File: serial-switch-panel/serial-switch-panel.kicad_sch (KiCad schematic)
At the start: 59 parts, among them J10 Conn_01x01, J11 Conn_01x01, J12 Conn_01x01, J13 Conn_01x01, J14 Conn_01x01, J15 Conn_01x01, J16 Conn_01x01, J17 Conn_01x01, J18 Conn_01x01, J2 2501551-4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

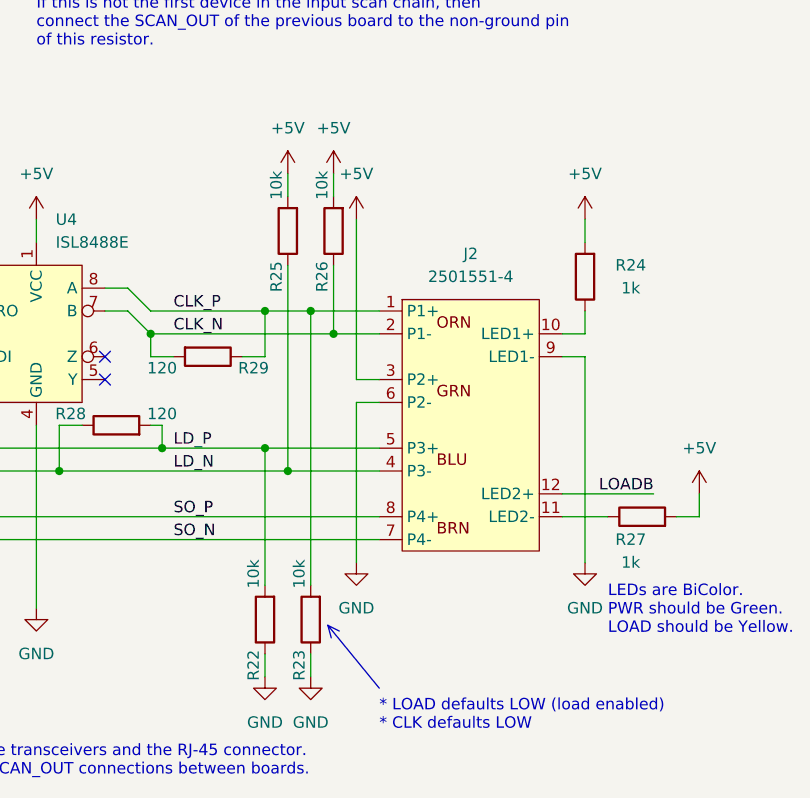
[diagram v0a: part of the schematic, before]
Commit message: Fix front-panel sch ERC
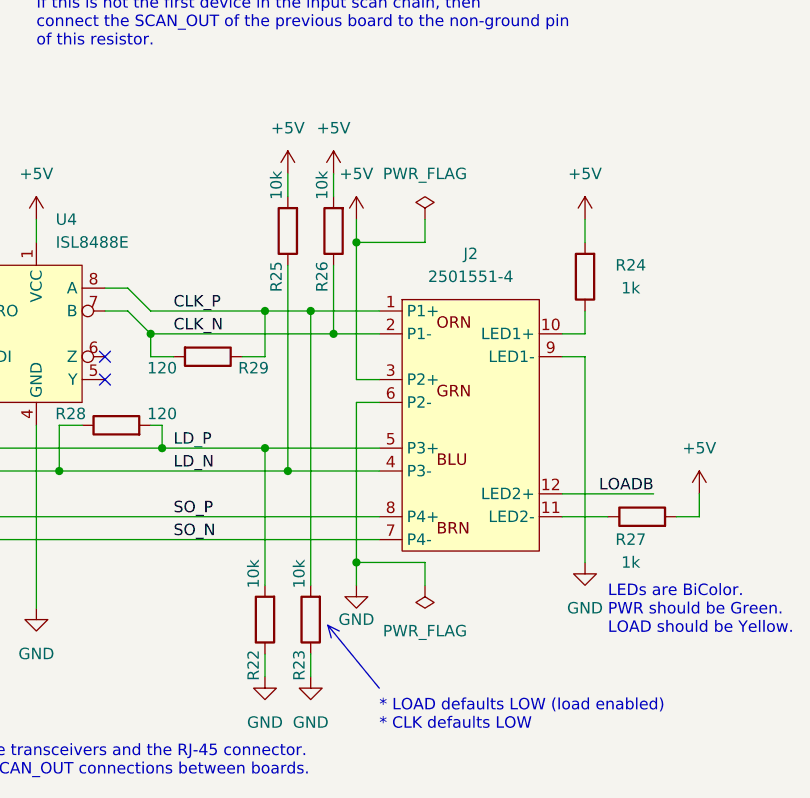
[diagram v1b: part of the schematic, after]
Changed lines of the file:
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@@
 	)
 	(junction
+		(at 119.38 167.64)
+		(diameter 0)
+		(color 0 0 0 0)
+	)
+	(junction
 		(at 116.84 142.24)
 		(diameter 0)
@@
 	)
 	(junction
+		(at 119.38 132.08)
+		(diameter 0)
+		(color 0 0 0 0)
+	)
+	(junction
 		(at 60.96 86.36)
 		(diameter 0)
@@
 	(wire
 		(pts
+			(xy 127 129.54) (xy 127 132.08)
+		)
+		(stroke
+			(width 0)
+			(type default)
+		)
+	)
+	(wire
+		(pts
 			(xy 30.48 58.42) (xy 33.02 58.42)
 		)
@@
 	(wire
 		(pts
+			(xy 119.38 132.08) (xy 119.38 147.32)
+		)
+		(stroke
+			(width 0)
+			(type default)
+		)
+	)
+	(wire
+		(pts
 			(xy 30.48 66.04) (xy 33.02 66.04)
 		)
@@
 		)
 	)
+	(wire
+		(pts
+			(xy 119.38 170.18) (xy 119.38 167.64)
+		)
+		(stroke
+			(width 0)
+			(type default)
+		)
+	)
 	(polyline
 		(pts
@@
 	(wire
 		(pts
+			(xy 127 170.18) (xy 127 167.64)
+		)
+		(stroke
+			(width 0)
+			(type default)
+		)
+	)
+	(wire
+		(pts
 			(xy 116.84 142.24) (xy 121.92 142.24)
 		)
@@
 	(wire
 		(pts
+			(xy 127 167.64) (xy 119.38 167.64)
+		)
+		(stroke
+			(width 0)
+			(type default)
+		)
+	)
+	(wire
+		(pts
 			(xy 40.64 55.88) (xy 66.04 55.88)
 		)
@@
 	(wire
 		(pts
-			(xy 119.38 129.54) (xy 119.38 147.32)
+			(xy 119.38 129.54) (xy 119.38 132.08)
 		)
 		(stroke
@@
 	(wire
 		(pts
+			(xy 127 132.08) (xy 119.38 132.08)
+		)
+		(stroke
+			(width 0)
+			(type default)
+		)
+	)
+	(wire
+		(pts
 			(xy 96.52 142.24) (xy 116.84 142.24)
 		)
@@
 	(symbol
 		(lib_id "power:GND")
-		(at 119.38 167.64 0)
+		(at 119.38 170.18 0)
 		(unit 1)
 		(body_style 1)
@@
 		(in_pos_files yes)
 		(dnp no)
-		(fields_autoplaced yes)
 		(property "Reference" "#PWR022"
-			(at 119.38 173.99 0)
+			(at 119.38 176.53 0)
 			(hide yes)
 			(show_name no)
@@
 		)
 		(property "Value" "GND"
-			(at 119.38 172.72 0)
+			(at 119.38 173.99 0)
 			(show_name no)
 			(do_not_autoplace no)
@@
 		)
 		(property "Footprint" ""
-			(at 119.38 167.64 0)
+			(at 119.38 170.18 0)
 			(hide yes)
 			(show_name no)
@@
 		)
 		(property "Datasheet" ""
-			(at 119.38 167.64 0)
+			(at 119.38 170.18 0)
 			(hide yes)
 			(show_name no)
@@
 		)
 		(property "Description" "Power symbol creates a global label with name \"GND\" , ground"
-			(at 119.38 167.64 0)
+			(at 119.38 170.18 0)
 			(hide yes)
 			(show_name no)
@@
 	)
 	(symbol
+		(lib_id "power:PWR_FLAG")
+		(at 127 170.18 0)
+		(mirror x)
+		(unit 1)
+		(body_style 1)
+		(exclude_from_sim no)
+		(in_bom yes)
+		(on_board yes)
+		(in_pos_files yes)
+		(dnp no)
+		(fields_autoplaced yes)
+		(property "Reference" "#FLG02"
+			(at 127 172.085 0)
+			(hide yes)
+			(show_name no)
+			(do_not_autoplace no)
+			(effects
+				(font
+					(size 1.27 1.27)
+				)
+			)
+		)
+		(property "Value" "PWR_FLAG"
+			(at 127 175.26 0)
+			(show_name no)
+			(do_not_autoplace no)
+			(effects
+				(font
+					(size 1.27 1.27)
+				)
+			)
+		)
+		(property "Footprint" ""
+			(at 127 170.18 0)
+			(hide yes)
+			(show_name no)
+			(do_not_autoplace no)
+			(effects
+				(font
+					(size 1.27 1.27)
+				)
+			)
+		)
+		(property "Datasheet" ""
+			(at 127 170.18 0)
+			(hide yes)
+			(show_name no)
+			(do_not_autoplace no)
+			(effects
+				(font
+					(size 1.27 1.27)
+				)
+			)
+		)
+		(property "Description" "Special symbol for telling ERC where power comes from"
+			(at 127 170.18 0)
+			(hide yes)
+			(show_name no)
+			(do_not_autoplace no)
+			(effects
+				(font
+					(size 1.27 1.27)
+				)
+			)
+		)
+		(pin "1"
+		)
+		(instances
+			(project "serial-switch-panel"
+				(path "/6e8e0d39-e51b-4511-a712-1d92a774977f"
+					(reference "#FLG02")
+					(unit 1)
+				)
+			)
+		)
+	)
+	(symbol
 		(lib_id "CUSTOM:C_Polarized")
 		(at 243.84 144.78 0)
@@
 					(unit 1)
 				)
+			)
+		)
+	)
+	(symbol
+		(lib_id "power:PWR_FLAG")
+		(at 127 129.54 0)
+		(unit 1)
+		(body_style 1)
+		(exclude_from_sim no)
+		(in_bom yes)
+		(on_board yes)
+		(in_pos_files yes)
+		(dnp no)
+		(fields_autoplaced yes)
+		(property "Reference" "#FLG01"
+			(at 127 127.635 0)
+			(hide yes)
+			(show_name no)
+			(do_not_autoplace no)
+			(effects
+				(font
+					(size 1.27 1.27)
+				)
+			)
+		)
+		(property "Value" "PWR_FLAG"
+			(at 127 124.46 0)
+			(show_name no)
+			(do_not_autoplace no)
+			(effects
+				(font
+					(size 1.27 1.27)
+				)
+			)
+		)
+		(property "Footprint" ""
+			(at 127 129.54 0)
+			(hide yes)
+			(show_name no)
+			(do_not_autoplace no)
+			(effects
+				(font
+					(size 1.27 1.27)
+				)
+			)
+		)
+		(property "Datasheet" ""
+			(at 127 129.54 0)
+			(hide yes)
+			(show_name no)
+			(do_not_autoplace no)
+			(effects
+				(font
+					(size 1.27 1.27)
+				)
+			)
+		)
+		(property "Description" "Special symbol for telling ERC where power comes from"
+			(at 127 129.54 0)
+			(hide yes)
+			(show_name no)
+			(do_not_autoplace no)
+			(effects
+				(font
+					(size 1.27 1.27)
+				)
+			)
+		)
+		(pin "1"
+		)
+		(instances
+			(project ""
+				(path "/6e8e0d39-e51b-4511-a712-1d92a774977f"
+					(reference "#FLG01")
+					(unit 1)
+				)

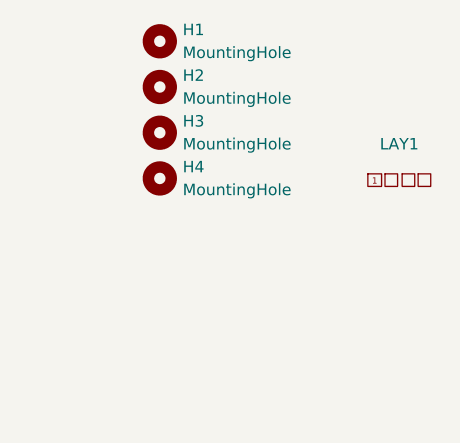
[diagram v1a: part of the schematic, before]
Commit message: Rough front-panel placement
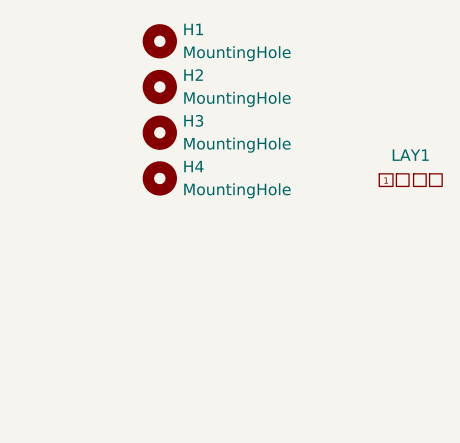
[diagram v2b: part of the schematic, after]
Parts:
- removed LAY1: (no value), custom_footprints:Layer_Indicator_4, symbol Custom:Layer_Indicator
- added LAY1: (no value), Symbol:LayerMarker_2_3.81x2.54mm_TextH1mm_P1.27mm_BottomMirrored, symbol CUSTOM:Layer_Indicator
- J10, J11, J12, J13, J14, J15, J16, J17, J18, J3, J4, J5, J6, J7, J8, J9: footprint (none) -> CUSTOM:Pin_D1.0mm
- J2: footprint (none) -> CUSTOM:2501551-4
- U1: footprint (none) -> Package_SO:Texas_DYY0016A_TSOT-23-16_2x4.2mm_P0.5mm
- U3: footprint (none) -> Package_SO:TSOP-5_1.65x3.05mm_P0.95mm
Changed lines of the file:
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@@
 			)
 		)
-		(property "Footprint" ""
+		(property "Footprint" "CUSTOM:Pin_D1.0mm"
 			(at 241.3 106.68 0)
 			(hide yes)
@@
 			)
 		)
-		(property "Footprint" ""
+		(property "Footprint" "CUSTOM:Pin_D1.0mm"
 			(at 48.26 170.18 0)
 			(hide yes)
@@
 			)
 		)
-		(property "Footprint" ""
+		(property "Footprint" "CUSTOM:Pin_D1.0mm"
 			(at 25.4 58.42 0)
 			(hide yes)
@@
 	)
 	(symbol
+		(lib_id "CUSTOM:Layer_Indicator")
+		(at 271.78 38.1 0)
+		(unit 1)
+		(body_style 1)
+		(exclude_from_sim no)
+		(in_bom no)
+		(on_board yes)
+		(in_pos_files yes)
+		(dnp no)
+		(fields_autoplaced yes)
+		(property "Reference" "LAY1"
+			(at 271.7165 35.56 0)
+			(show_name no)
+			(do_not_autoplace no)
+			(effects
+				(font
+					(size 1.27 1.27)
+				)
+			)
+		)
+		(property "Value" ""
+			(at 271.7165 35.56 0)
+			(show_name no)
+			(do_not_autoplace no)
+			(effects
+				(font
+					(size 1.27 1.27)
+				)
+			)
+		)
+		(property "Footprint" "Symbol:LayerMarker_2_3.81x2.54mm_TextH1mm_P1.27mm_BottomMirrored"
+			(at 270.764 36.322 0)
+			(hide yes)
+			(show_name no)
+			(do_not_autoplace no)
+			(effects
+				(font
+					(size 1.27 1.27)
+				)
+			)
+		)
+		(property "Datasheet" ""
+			(at 270.764 36.322 0)
+			(hide yes)
+			(show_name no)
+			(do_not_autoplace no)
+			(effects
+				(font
+					(size 1.27 1.27)
+				)
+			)
+		)
+		(property "Description" ""
+			(at 270.764 36.322 0)
+			(hide yes)
+			(show_name no)
+			(do_not_autoplace no)
+			(effects
+				(font
+					(size 1.27 1.27)
+				)
+			)
+		)
+		(instances
+			(project ""
+				(path "/6e8e0d39-e51b-4511-a712-1d92a774977f"
+					(reference "LAY1")
+					(unit 1)
+				)
+			)
+		)
+	)
+	(symbol
 		(lib_id "CUSTOM:R")
 		(at 71.12 78.74 180)
@@
 			)
 		)
-		(property "Footprint" ""
+		(property "Footprint" "CUSTOM:Pin_D1.0mm"
 			(at 129.54 50.8 0)
 			(hide yes)
@@
 			)
 		)
-		(property "Footprint" ""
+		(property "Footprint" "CUSTOM:Pin_D1.0mm"
 			(at 25.4 63.5 0)
 			(hide yes)
@@
 			)
 		)
-		(property "Footprint" ""
+		(property "Footprint" "CUSTOM:Pin_D1.0mm"
 			(at 25.4 48.26 0)
 			(hide yes)
@@
 			)
 		)
-		(property "Footprint" ""
+		(property "Footprint" "CUSTOM:Pin_D1.0mm"
 			(at 25.4 55.88 0)
 			(hide yes)
@@
 			)
 		)
-		(property "Footprint" ""
+		(property "Footprint" "CUSTOM:2501551-4"
 			(at 132.08 152.4 0)
 			(hide yes)
@@
 			)
 		)
-		(property "Footprint" ""
+		(property "Footprint" "Package_SO:Texas_DYY0016A_TSOT-23-16_2x4.2mm_P0.5mm"
 			(at 109.22 63.5 0)
 			(hide yes)
@@
 			)
 		)
-		(property "Footprint" ""
+		(property "Footprint" "CUSTOM:Pin_D1.0mm"
 			(at 25.4 50.8 0)
 			(hide yes)
@@
 			)
 		)
-		(property "Footprint" ""
+		(property "Footprint" "CUSTOM:Pin_D1.0mm"
 			(at 25.4 101.6 0)
 			(hide yes)
@@
 			)
 		)
-		(property "Footprint" ""
+		(property "Footprint" "CUSTOM:Pin_D1.0mm"
 			(at 25.4 106.68 0)
 			(hide yes)
@@
 			)
 		)
-		(property "Footprint" ""
+		(property "Footprint" "CUSTOM:Pin_D1.0mm"
 			(at 73.66 132.08 0)
 			(hide yes)
@@
 			)
 		)
-		(property "Footprint" ""
+		(property "Footprint" "CUSTOM:Pin_D1.0mm"
 			(at 25.4 60.96 0)
 			(hide yes)
@@
 	)
 	(symbol
-		(lib_id "Custom:Layer_Indicator")
-		(at 270.51 38.1 0)
-		(unit 1)
-		(body_style 1)
-		(exclude_from_sim no)
-		(in_bom no)
-		(on_board yes)
-		(in_pos_files yes)
-		(dnp no)
-		(fields_autoplaced yes)
-		(property "Reference" "LAY1"
-			(at 270.4465 34.29 0)
-			(show_name no)
-			(do_not_autoplace no)
-			(effects
-				(font
-					(size 1.27 1.27)
-				)
-			)
-		)
-		(property "Value" ""
-			(at 270.4465 35.56 0)
-			(show_name no)
-			(do_not_autoplace no)
-			(effects
-				(font
-					(size 1.27 1.27)
-				)
-			)
-		)
-		(property "Footprint" "custom_footprints:Layer_Indicator_4"
-			(at 269.494 36.322 0)
-			(hide yes)
-			(show_name no)
-			(do_not_autoplace no)
-			(effects
-				(font
-					(size 1.27 1.27)
-				)
-			)
-		)
-		(property "Datasheet" ""
-			(at 269.494 36.322 0)
-			(hide yes)
-			(show_name no)
-			(do_not_autoplace no)
-			(effects
-				(font
-					(size 1.27 1.27)
-				)
-			)
-		)
-		(property "Description" ""
-			(at 269.494 36.322 0)
-			(hide yes)
-			(show_name no)
-			(do_not_autoplace no)
-			(effects
-				(font
-					(size 1.27 1.27)
-				)
-			)
-		)
-		(instances
-			(project "serial-switch-panel"
-				(path "/6e8e0d39-e51b-4511-a712-1d92a774977f"
-					(reference "LAY1")
-					(unit 1)
-				)
-			)
-		)
-	)
-	(symbol
 		(lib_id "CUSTOM:C")
 		(at 182.88 144.78 0)
@@
 			)
 		)
-		(property "Footprint" ""
+		(property "Footprint" "Package_SO:TSOP-5_1.65x3.05mm_P0.95mm"
 			(at 167.64 48.26 0)
 			(hide yes)
@@
 			)
 		)
-		(property "Footprint" ""
+		(property "Footprint" "CUSTOM:Pin_D1.0mm"
 			(at 48.26 149.86 0)
 			(hide yes)
@@
 			)
 		)
-		(property "Footprint" ""
+		(property "Footprint" "CUSTOM:Pin_D1.0mm"
 			(at 241.3 101.6 0)
 			(hide yes)
@@
 			)
 		)
-		(property "Footprint" ""
+		(property "Footprint" "CUSTOM:Pin_D1.0mm"
 			(at 25.4 53.34 0)
 			(hide yes)
@@
 			)
 		)
-		(property "Footprint" ""
+		(property "Footprint" "CUSTOM:Pin_D1.0mm"
 			(at 25.4 66.04 0)
 			(hide yes)

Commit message: [fp] Correct P4+/- swap in ethernet connector
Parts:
- C2: footprint Capacitor_SMD:C_1206_3216Metric -> Capacitor_THT:C_Radial_D8.0mm_H7.0mm_P3.50mm
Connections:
- net SO_N: now also J2.8 (P4-), U2.5 (Y); no longer J2.7 (P4-), U2.6 (Z)
- net SO_P: now also J2.7 (P4+), U2.6 (Z); no longer J2.8 (P4+), U2.5 (Y)
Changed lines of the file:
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@@
 	(wire
 		(pts
-			(xy 66.04 162.56) (xy 71.12 162.56)
-		)
-		(stroke
-			(width 0)
-			(type default)
-		)
-	)
-	(wire
-		(pts
 			(xy 66.04 157.48) (xy 86.36 157.48)
 		)
@@
 	(wire
 		(pts
-			(xy 73.66 165.1) (xy 121.92 165.1)
-		)
-		(stroke
-			(width 0)
-			(type default)
-		)
-	)
-	(wire
-		(pts
 			(xy 58.42 63.5) (xy 58.42 73.66)
 		)
@@
 	(wire
 		(pts
-			(xy 71.12 162.56) (xy 73.66 165.1)
-		)
-		(stroke
-			(width 0)
-			(type default)
-		)
-	)
-	(wire
-		(pts
 			(xy 58.42 86.36) (xy 60.96 86.36)
 		)
@@
 	(wire
 		(pts
+			(xy 66.04 162.56) (xy 121.92 162.56)
+		)
+		(stroke
+			(width 0)
+			(type default)
+		)
+	)
+	(wire
+		(pts
 			(xy 30.48 63.5) (xy 33.02 63.5)
 		)
@@
 	(wire
 		(pts
-			(xy 66.04 165.1) (xy 71.12 165.1)
-		)
-		(stroke
-			(width 0)
-			(type default)
-		)
-	)
-	(wire
-		(pts
 			(xy 121.92 45.72) (xy 152.4 45.72)
 		)
@@
 	(wire
 		(pts
+			(xy 66.04 165.1) (xy 121.92 165.1)
+		)
+		(stroke
+			(width 0)
+			(type default)
+		)
+	)
+	(wire
+		(pts
 			(xy 228.6 139.7) (xy 228.6 142.24)
 		)
@@
 	(wire
 		(pts
-			(xy 73.66 162.56) (xy 121.92 162.56)
-		)
-		(stroke
-			(width 0)
-			(type default)
-		)
-	)
-	(wire
-		(pts
 			(xy 40.64 66.04) (xy 55.88 66.04)
 		)
@@
 		)
 	)
-	(wire
-		(pts
-			(xy 71.12 165.1) (xy 73.66 162.56)
-		)
-		(stroke
-			(width 0)
-			(type default)
-		)
-	)
 	(label "IN_A"
 		(at 45.72 48.26 0)
@@
 			)
 		)
-		(property "Footprint" "Capacitor_SMD:C_1206_3216Metric"
+		(property "Footprint" "Capacitor_THT:C_Radial_D8.0mm_H7.0mm_P3.50mm"
 			(at 244.8052 148.59 0)
 			(hide yes)
